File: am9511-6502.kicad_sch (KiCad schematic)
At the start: 14 parts, among them J1 Conn_01x18_Pin, U1 AM9511A, U2 ATF16V8B, U3 74HC112, U4 ADA-TPS61040, U5 74HC123, X1 4 MHz

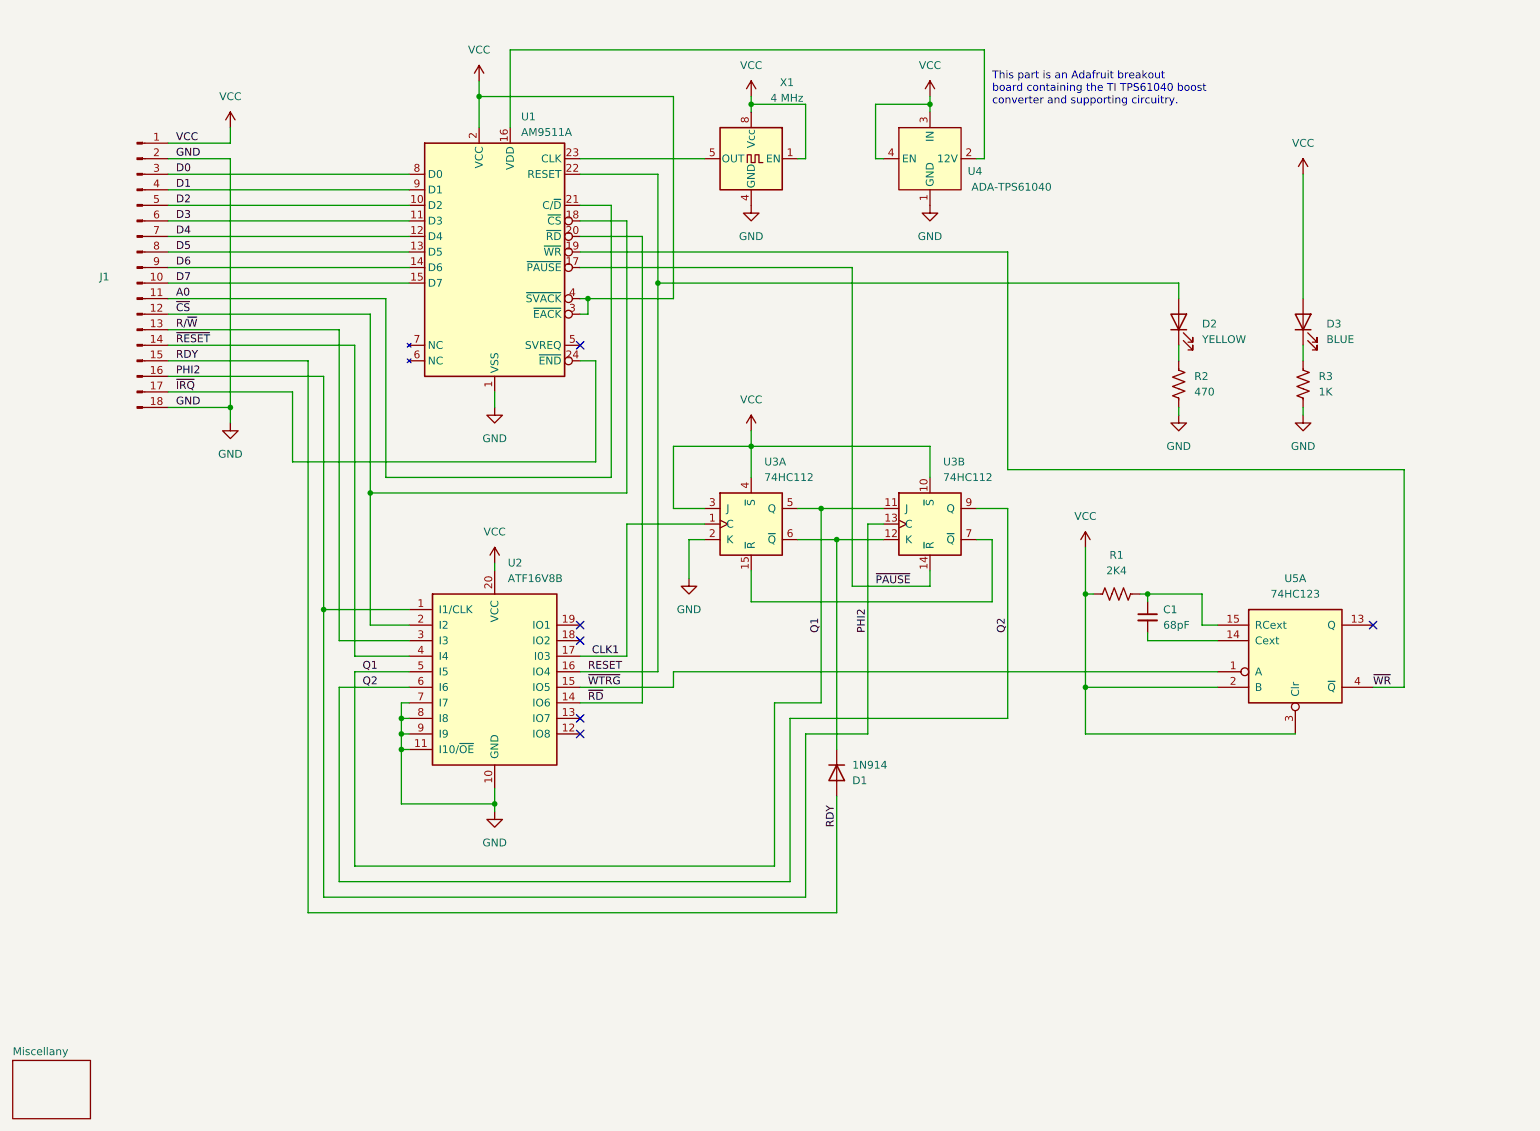
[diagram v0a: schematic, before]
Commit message: Add PAL-2 expansion connection and CS
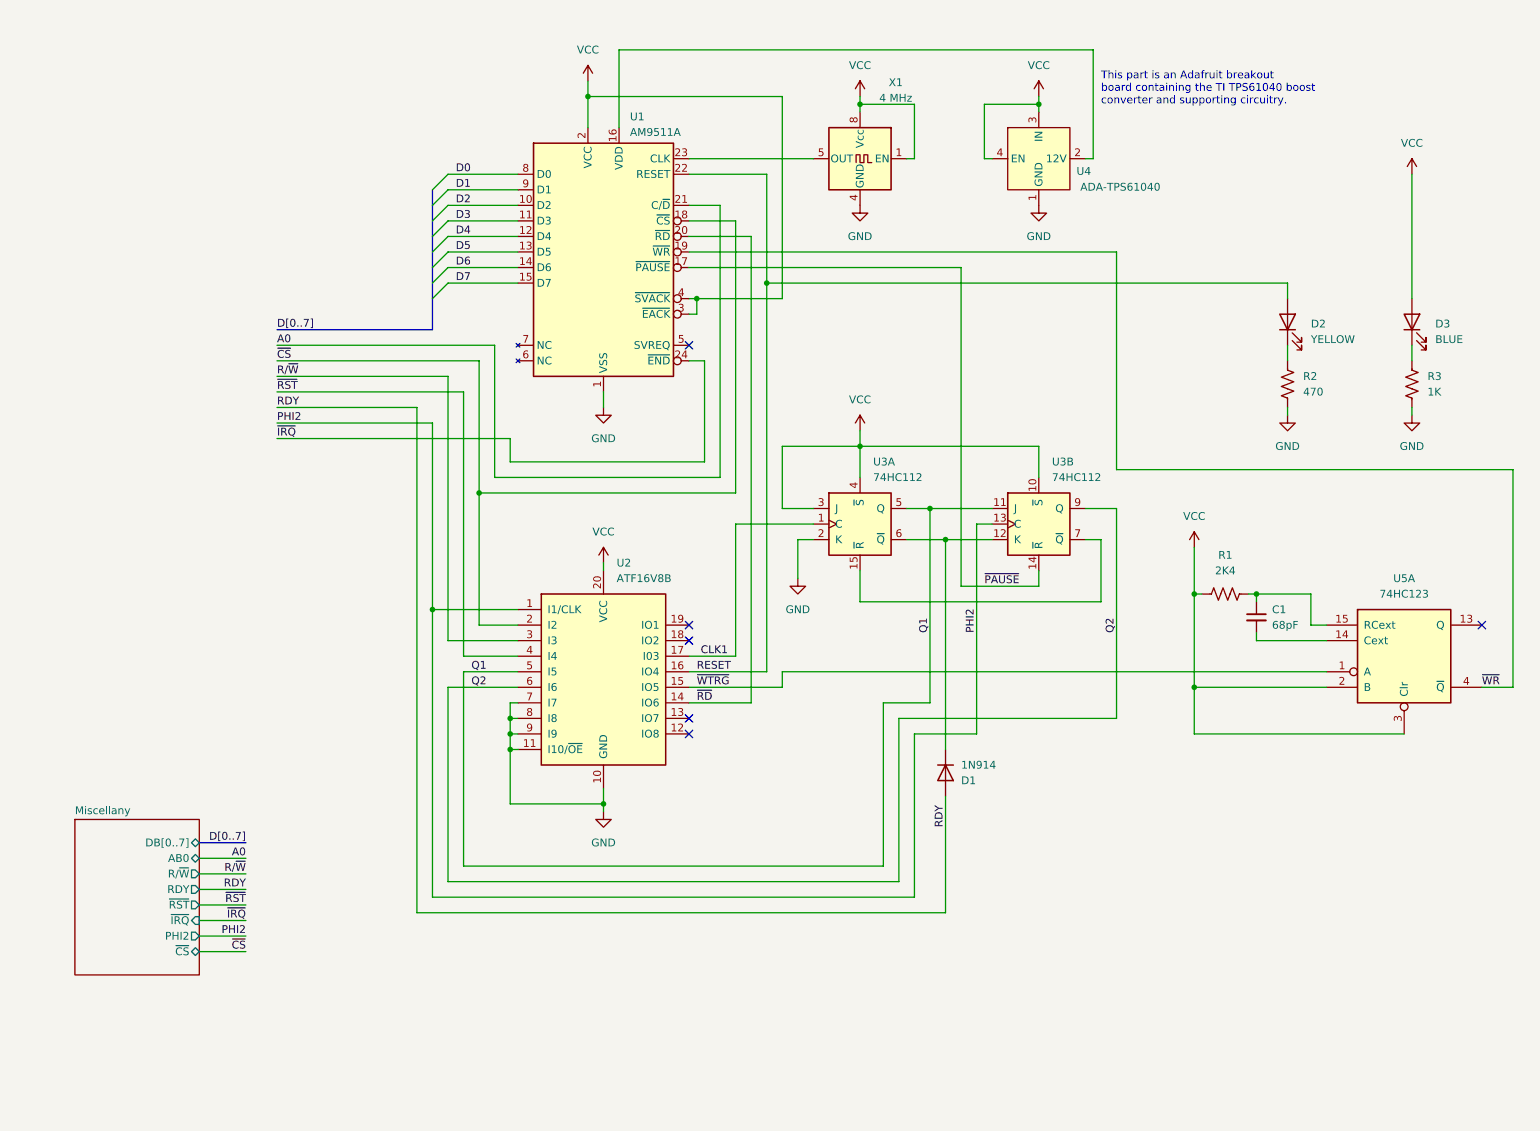
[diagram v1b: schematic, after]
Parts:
- removed J1: Conn_01x18_Pin, am9511-6502-footprints:PinHeader_1x18_P2.54mm_Horizontal, symbol Connector:Conn_01x18_Pin
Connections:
- net ~{RESET} renamed ~{RST}
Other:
- sheet Miscellany ports: added AB0, DB[0..7], PHI2, RDY, R/~{W}, ~{CS}, ~{IRQ}, ~{RST}; removed none
- title: AM9511 Interface for 6509 -> AM9511 Interface for PAL-2
- moved on the sheet: C1, D1, D2, D3, R1, R2, R3, U1, U2, U3A, U3B, U4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

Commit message: Initial PAL-2 version
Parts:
- removed R3: 1K, Resistor_THT:R_Axial_DIN0207_L6.3mm_D2.5mm_P7.62mm_Horizontal, symbol Device:R_US
- removed U4: ADA-TPS61040, am9511-6502-footprints:ADA-TPS61040, symbol am9511-6502-symbols:ADA-TPS61040
- removed X1: 4 MHz, Oscillator:Oscillator_DIP-8, symbol Oscillator:CXO_DIP8
- added JP2: IRQ_ENABLE, Connector_PinHeader_2.54mm:PinHeader_1x02_P2.54mm_Vertical, symbol Jumper:Jumper_2_Open
- added R5: 2K7, Resistor_THT:R_Axial_DIN0207_L6.3mm_D2.5mm_P7.62mm_Horizontal, symbol Device:R_US
- added R6: 470, Resistor_THT:R_Axial_DIN0207_L6.3mm_D2.5mm_P7.62mm_Horizontal, symbol Device:R_US
- added U4: DD1718PA, am9511-6502-footprints:DD1718PA, symbol am9511-6502-symbols:DD1718PA
- added U8: 74LS04, Package_DIP:DIP-14_W7.62mm_Socket, symbol 74xx:74HC04
- D2: value YELLOW -> RESET
- D3: value BLUE -> END
- U3: value 74HC112 -> 74LS112
- U5: value 74HC123 -> 74LS123
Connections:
- net GND: now also R2.1, R6.1, U4.2 (GND), U4.4 (GND); no longer R2.2
- net VCC: now also R5.1, U4.1 (V_{in}); no longer D3.2 (A)
- net ~{IRQ}: now also U8.10; no longer U1.24 (~{END})
- net at D2.1 (K): now also R2.2; no longer R2.1
- net at U1.16 (VDD): now also U4.3 (V_{o+})
- net at D3.1 (K): now also R6.2
- net CLOCK: now reaches U1.23 (CLK)
- new net: D3.2 (A), U8.11, U8.8
- new net: JP2.2 (B), R5.2, U8.9
- new net: JP2.1 (A), U1.24 (~{END})
- no-connect marks 6 -> 7
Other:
- sheet Miscellany renamed PAL-2 Interface
- added sheet Clock (clock.kicad_sch)
- note added: "This part is a DD1718PA breakout board containing the +5V to +12V DC-DC converter and supporting circuitry."
- note removed: "This part is an Adafruit breakout board containing the TI TPS61040 boost converter and supporting circuitry."
- moved on the sheet: C1, D2, R1, R2, U3A, U3B, U5A

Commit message: First manufacturing prototype
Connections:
- net ~{IRQ}: now also JP2.1 (A); no longer U8.10
- net at R5.2, U8.9: now also U1.24 (~{END}); no longer JP2.2 (B)
- new net: JP2.2 (B), U8.10
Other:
- moved on the sheet: D3, JP2, R5, R6, U8D, U8E

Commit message: Minor improvements to schematic
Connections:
- net GND: now also C1.2, U5.14 (Cext)
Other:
- moved on the sheet: C1, R1
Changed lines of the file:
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@@
 	)
 	(junction
-		(at 217.17 116.84)
+		(at 217.17 121.92)
 		(diameter 0)
 		(color 0 0 0 0)
@@
 	)
 	(junction
+		(at 217.17 113.03)
+		(diameter 0)
+		(color 0 0 0 0)
+	)
+	(junction
 		(at 90.17 95.25)
 		(diameter 0)
@@
 	)
 	(junction
-		(at 207.01 116.84)
-		(diameter 0)
-		(color 0 0 0 0)
-	)
-	(junction
 		(at 82.55 116.84)
 		(diameter 0)
@@
 	)
 	(junction
+		(at 207.01 113.03)
+		(diameter 0)
+		(color 0 0 0 0)
+	)
+	(junction
 		(at 207.01 132.08)
 		(diameter 0)
@@
 	(wire
 		(pts
-			(xy 217.17 116.84) (xy 226.06 116.84)
-		)
-		(stroke
-			(width 0)
-			(type default)
-		)
-	)
-	(wire
-		(pts
 			(xy 181.61 92.71) (xy 181.61 97.79)
 		)
@@
 	(wire
 		(pts
+			(xy 217.17 113.03) (xy 217.17 115.57)
+		)
+		(stroke
+			(width 0)
+			(type default)
+		)
+	)
+	(wire
+		(pts
 			(xy 204.47 54.61) (xy 204.47 76.2)
 		)
@@
 	(wire
 		(pts
-			(xy 207.01 116.84) (xy 207.01 132.08)
+			(xy 207.01 113.03) (xy 207.01 132.08)
 		)
 		(stroke
@@
 	(wire
 		(pts
-			(xy 215.9 116.84) (xy 217.17 116.84)
-		)
-		(stroke
-			(width 0)
-			(type default)
-		)
-	)
-	(wire
-		(pts
-			(xy 217.17 124.46) (xy 228.6 124.46)
-		)
-		(stroke
-			(width 0)
-			(type default)
-		)
-	)
-	(wire
-		(pts
-			(xy 207.01 116.84) (xy 208.28 116.84)
+			(xy 215.9 113.03) (xy 217.17 113.03)
+		)
+		(stroke
+			(width 0)
+			(type default)
+		)
+	)
+	(wire
+		(pts
+			(xy 207.01 113.03) (xy 208.28 113.03)
 		)
 		(stroke
@@
 	(wire
 		(pts
+			(xy 217.17 121.92) (xy 217.17 120.65)
+		)
+		(stroke
+			(width 0)
+			(type default)
+		)
+	)
+	(wire
+		(pts
 			(xy 139.7 33.02) (xy 107.95 33.02)
 		)
@@
 	(wire
 		(pts
-			(xy 217.17 124.46) (xy 217.17 123.19)
-		)
-		(stroke
-			(width 0)
-			(type default)
-		)
-	)
-	(wire
-		(pts
-			(xy 207.01 109.22) (xy 207.01 116.84)
+			(xy 217.17 123.19) (xy 217.17 121.92)
+		)
+		(stroke
+			(width 0)
+			(type default)
+		)
+	)
+	(wire
+		(pts
+			(xy 207.01 109.22) (xy 207.01 113.03)
+		)
+		(stroke
+			(width 0)
+			(type default)
+		)
+	)
+	(wire
+		(pts
+			(xy 226.06 124.46) (xy 228.6 124.46)
 		)
 		(stroke
@@
 	(wire
 		(pts
-			(xy 226.06 121.92) (xy 228.6 121.92)
-		)
-		(stroke
-			(width 0)
-			(type default)
-		)
-	)
-	(wire
-		(pts
 			(xy 85.09 55.88) (xy 96.52 55.88)
 		)
@@
 	(wire
 		(pts
-			(xy 226.06 121.92) (xy 226.06 116.84)
+			(xy 228.6 121.92) (xy 228.6 113.03)
 		)
 		(stroke
@@
 	(wire
 		(pts
-			(xy 217.17 116.84) (xy 217.17 118.11)
-		)
-		(stroke
-			(width 0)
-			(type default)
-		)
-	)
-	(wire
-		(pts
 			(xy 137.16 55.88) (xy 189.23 55.88)
 		)
@@
 	(wire
 		(pts
+			(xy 217.17 121.92) (xy 226.06 121.92)
+		)
+		(stroke
+			(width 0)
+			(type default)
+		)
+	)
+	(wire
+		(pts
 			(xy 189.23 36.83) (xy 189.23 38.1)
 		)
@@
 		)
 	)
+	(wire
+		(pts
+			(xy 217.17 113.03) (xy 228.6 113.03)
+		)
+		(stroke
+			(width 0)
+			(type default)
+		)
+	)
 	(bus
 		(pts
@@
 		(pts
 			(xy 80.01 83.82) (xy 80.01 166.37)
+		)
+		(stroke
+			(width 0)
+			(type default)
+		)
+	)
+	(wire
+		(pts
+			(xy 226.06 121.92) (xy 226.06 124.46)
 		)
 		(stroke
@@
 	)
 	(symbol
+		(lib_id "power:GND")
+		(at 217.17 123.19 0)
+		(unit 1)
+		(exclude_from_sim no)
+		(in_bom yes)
+		(on_board yes)
+		(dnp no)
+		(fields_autoplaced yes)
+		(property "Reference" "#PWR036"
+			(at 217.17 129.54 0)
+			(effects
+				(font
+					(size 1.27 1.27)
+				)
+				(hide yes)
+			)
+		)
+		(property "Value" "GND"
+			(at 217.17 128.27 0)
+			(effects
+				(font
+					(size 1.27 1.27)
+				)
+			)
+		)
+		(property "Footprint" ""
+			(at 217.17 123.19 0)
+			(effects
+				(font
+					(size 1.27 1.27)
+				)
+				(hide yes)
+			)
+		)
+		(property "Datasheet" ""
+			(at 217.17 123.19 0)
+			(effects
+				(font
+					(size 1.27 1.27)
+				)
+				(hide yes)
+			)
+		)
+		(property "Description" "Power symbol creates a global label with name \"GND\" , ground"
+			(at 217.17 123.19 0)
+			(effects
+				(font
+					(size 1.27 1.27)
+				)
+				(hide yes)
+			)
+		)
+		(pin "1"
+		)
+		(instances
+			(project "am9511-6502"
+				(path "/492d2c5d-68ab-43c4-8db3-0d52dc374f84"
+					(reference "#PWR036")
+					(unit 1)
+				)
+			)
+		)
+	)
+	(symbol
 		(lib_id "power:VCC")
 		(at 110.49 109.22 0)
@@
 	(symbol
 		(lib_id "Device:R_US")
-		(at 212.09 116.84 90)
+		(at 212.09 113.03 90)
 		(unit 1)
 		(exclude_from_sim no)
@@
 		(fields_autoplaced yes)
 		(property "Reference" "R1"
-			(at 212.09 110.49 90)
+			(at 212.09 106.68 90)
 			(effects
 				(font
@@
 		)
 		(property "Value" "2K4"
-			(at 212.09 113.03 90)
+			(at 212.09 109.22 90)
 			(effects
 				(font
@@
 		)
 		(property "Footprint" "Resistor_THT:R_Axial_DIN0207_L6.3mm_D2.5mm_P7.62mm_Horizontal"
-			(at 212.344 115.824 90)
+			(at 212.344 112.014 90)
 			(effects
 				(font
@@
 		)
 		(property "Datasheet" "~"
-			(at 212.09 116.84 0)
+			(at 212.09 113.03 0)
 			(effects
 				(font
@@
 		)
 		(property "Description" "Resistor, US symbol"
-			(at 212.09 116.84 0)
+			(at 212.09 113.03 0)
 			(effects
 				(font
@@
 	(symbol
 		(lib_id "Device:C_Small")
-		(at 217.17 120.65 0)
+		(at 217.17 118.11 0)
 		(unit 1)
 		(exclude_from_sim no)
@@
 		(dnp no)
 		(property "Reference" "C1"
+			(at 219.71 116.8462 0)
+			(effects
+				(font
+					(size 1.27 1.27)
+				)
+				(justify left)
+			)
+		)
+		(property "Value" "68pF"
 			(at 219.71 119.3862 0)
 			(effects
@@
 			)
 		)
-		(property "Value" "68pF"
-			(at 219.71 121.9262 0)
-			(effects
-				(font
-					(size 1.27 1.27)
-				)
-				(justify left)
-			)
-		)
 		(property "Footprint" "Capacitor_THT:C_Disc_D5.0mm_W2.5mm_P5.00mm"
-			(at 217.17 120.65 0)
+			(at 217.17 118.11 0)
 			(effects
 				(font
@@
 		)
 		(property "Datasheet" "~"
-			(at 217.17 120.65 0)
+			(at 217.17 118.11 0)
 			(effects
 				(font
@@
 		)
 		(property "Description" "Unpolarized capacitor, small symbol"
-			(at 217.17 120.65 0)
-			(effects
-				(font
+			(at 217.17 118.11 0)
+			(effects
+				(font

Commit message: Minor improvements
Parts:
- removed R5: 2K7, Resistor_THT:R_Axial_DIN0207_L6.3mm_D2.5mm_P7.62mm_Horizontal, symbol Device:R_US
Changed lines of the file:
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@@
-	)
-	(junction
-		(at 181.61 76.2)
-		(diameter 0)
-		(color 0 0 0 0)
 	)
 	(junction
@@
 	(wire
 		(pts
-			(xy 181.61 63.5) (xy 181.61 64.77)
-		)
-		(stroke
-			(width 0)
-			(type default)
-		)
-	)
-	(wire
-		(pts
-			(xy 124.46 76.2) (xy 181.61 76.2)
+			(xy 124.46 76.2) (xy 187.96 76.2)
 		)
 		(stroke
@@
 	(wire
 		(pts
-			(xy 187.96 76.2) (xy 181.61 76.2)
-		)
-		(stroke
-			(width 0)
-			(type default)
-		)
-	)
-	(wire
-		(pts
 			(xy 204.47 45.72) (xy 204.47 46.99)
 		)
@@
 		(pts
 			(xy 152.4 92.71) (xy 152.4 97.79)
-		)
-		(stroke
-			(width 0)
-			(type default)
-		)
-	)
-	(wire
-		(pts
-			(xy 181.61 72.39) (xy 181.61 76.2)
 		)
 		(stroke
@@
 	)
 	(symbol
-		(lib_id "power:VCC")
-		(at 181.61 63.5 0)
-		(unit 1)
-		(exclude_from_sim no)
-		(in_bom yes)
-		(on_board yes)
-		(dnp no)
-		(property "Reference" "#PWR09"
-			(at 181.61 67.31 0)
-			(effects
-				(font
-					(size 1.27 1.27)
-				)
-				(hide yes)
-			)
-		)
-		(property "Value" "VCC"
-			(at 185.42 62.23 0)
-			(effects
-				(font
-					(size 1.27 1.27)
-				)
-			)
-		)
-		(property "Footprint" ""
-			(at 181.61 63.5 0)
-			(effects
-				(font
-					(size 1.27 1.27)
-				)
-				(hide yes)
-			)
-		)
-		(property "Datasheet" ""
-			(at 181.61 63.5 0)
-			(effects
-				(font
-					(size 1.27 1.27)
-				)
-				(hide yes)
-			)
-		)
-		(property "Description" "Power symbol creates a global label with name \"VCC\""
-			(at 181.61 63.5 0)
-			(effects
-				(font
-					(size 1.27 1.27)
-				)
-				(hide yes)
-			)
-		)
-		(pin "1"
-		)
-		(instances
-			(project "am9511-6502"
-				(path "/492d2c5d-68ab-43c4-8db3-0d52dc374f84"
-					(reference "#PWR09")
-					(unit 1)
-				)
-			)
-		)
-	)
-	(symbol
 		(lib_id "Device:R_US")
 		(at 212.09 113.03 90)
@@
 					(unit 1)
 				)
-			)
-		)
-	)
-	(symbol
-		(lib_id "Device:R_US")
-		(at 181.61 68.58 0)
-		(unit 1)
-		(exclude_from_sim no)
-		(in_bom yes)
-		(on_board yes)
-		(dnp no)
-		(fields_autoplaced yes)
-		(property "Reference" "R5"
-			(at 184.15 67.3099 0)
-			(effects
-				(font
-					(size 1.27 1.27)
-				)
-				(justify left)
-			)
-		)
-		(property "Value" "2K7"
-			(at 184.15 69.8499 0)
-			(effects
-				(font
-					(size 1.27 1.27)
-				)
-				(justify left)
-			)
-		)
-		(property "Footprint" "Resistor_THT:R_Axial_DIN0207_L6.3mm_D2.5mm_P7.62mm_Horizontal"
-			(at 182.626 68.834 90)
-			(effects
-				(font
-					(size 1.27 1.27)
-				)
-				(hide yes)
-			)
-		)
-		(property "Datasheet" "~"
-			(at 181.61 68.58 0)
-			(effects
-				(font
-					(size 1.27 1.27)
-				)
-				(hide yes)
-			)
-		)
-		(property "Description" "Resistor, US symbol"
-			(at 181.61 68.58 0)
-			(effects
-				(font
-					(size 1.27 1.27)
-				)
-				(hide yes)
-			)
-		)
-		(pin "2"
-		)
-		(pin "1"
-		)
-		(instances
-			(project "am9511-6502"
-				(path "/492d2c5d-68ab-43c4-8db3-0d52dc374f84"
-					(reference "R5")
-					(unit 1)
-				)
